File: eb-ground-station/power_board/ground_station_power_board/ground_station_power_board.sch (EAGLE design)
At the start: 73 parts, among them J1 CONN_20X2SHROUDED, Q1 SQJ459EP_MOSFET_P_CHAN, Q15 DMN61D8LVT-DUAL-N-CHANNEL-MOS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, Q17 DMN61D8LVT-DUAL-N-CHANNEL-MOS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, Q18 DMN61D8LVT-DUAL-N-CHANNEL-MOS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, Q2 SQJ459EP_MOSFET_P_CHAN, Q22 TC4427-FET-GATE-DRVR, Q23 TC4427-FET-GATE-DRVR, Q24 TC4427-FET-GATE-DRVR, Q3 SQJ459EP_MOSFET_P_CHAN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

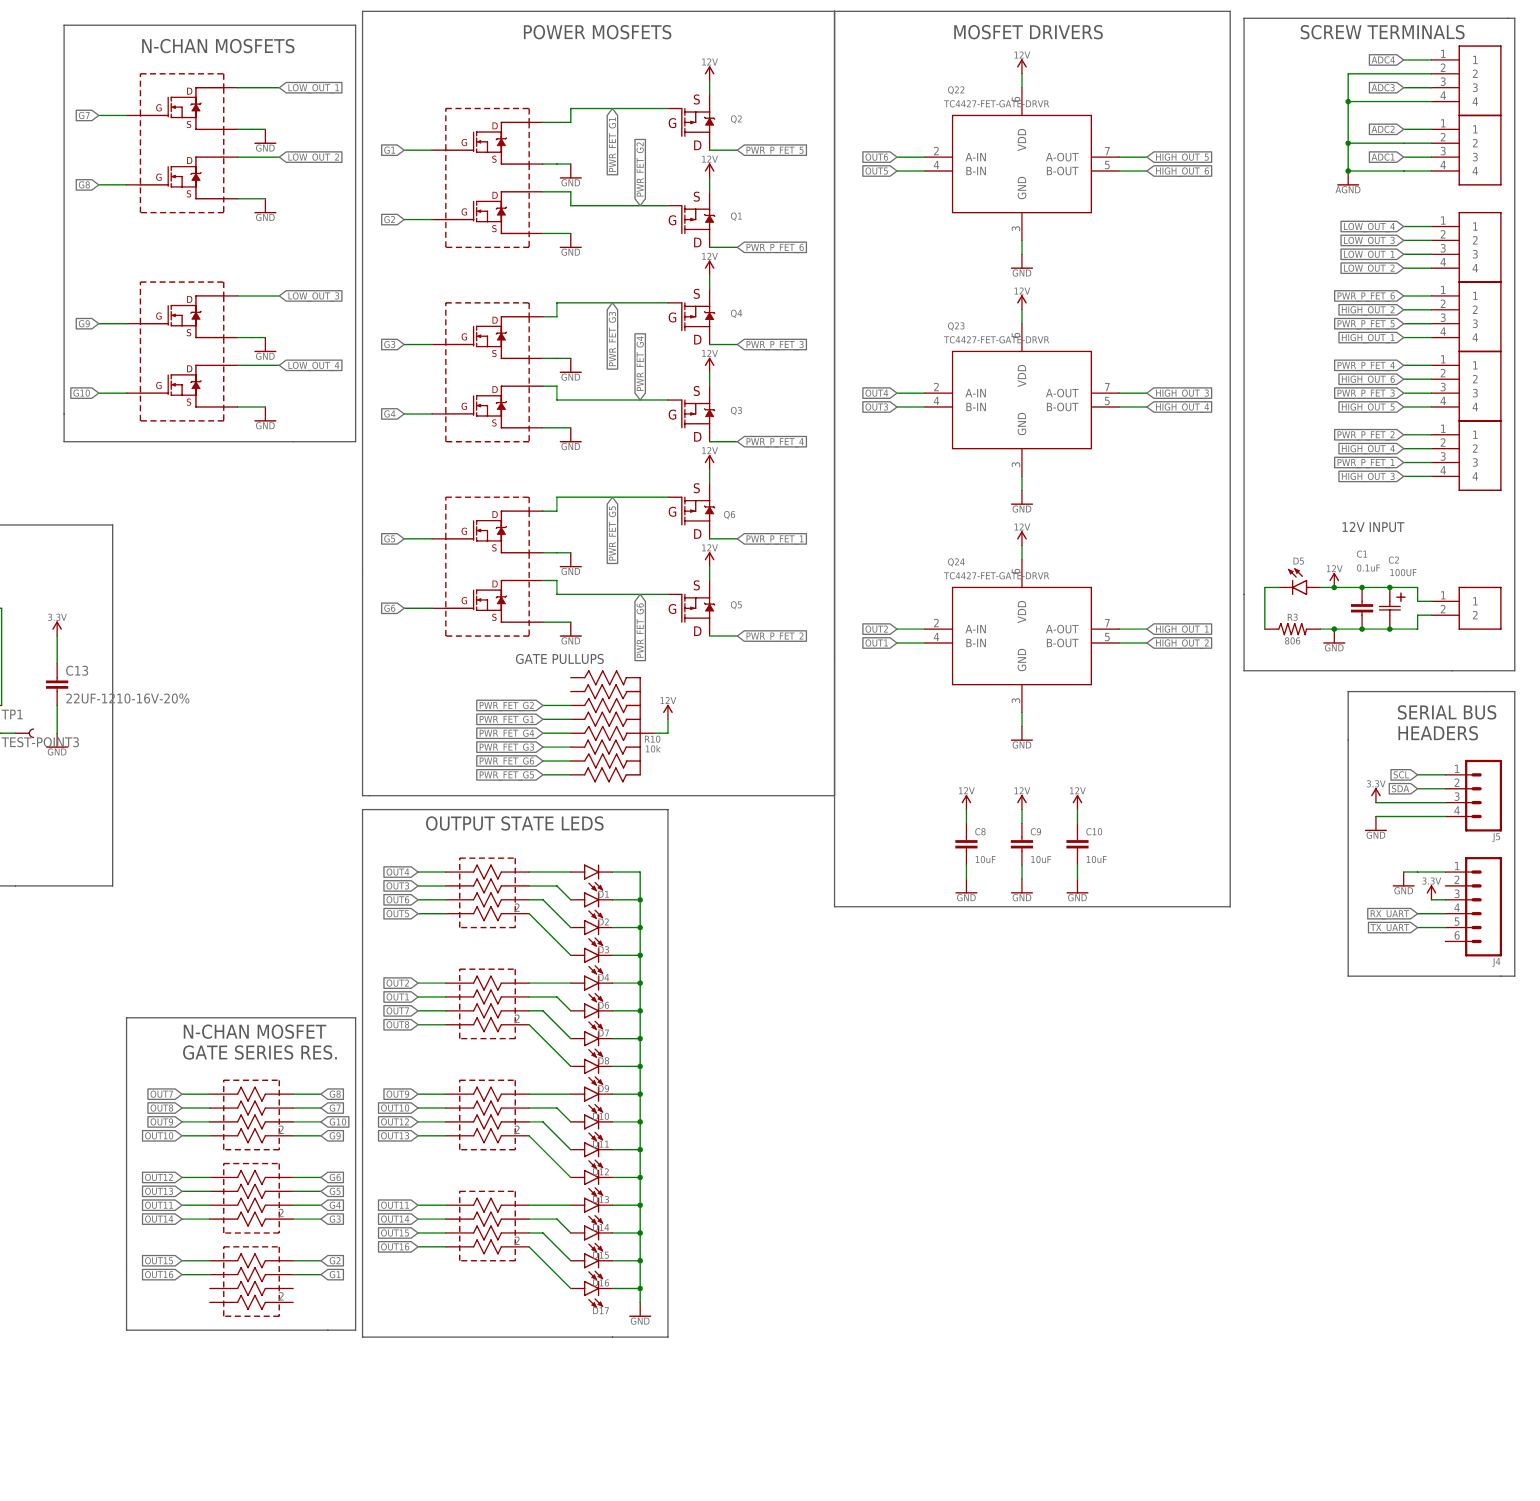
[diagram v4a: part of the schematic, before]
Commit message: Updated for 2  5V mosfets
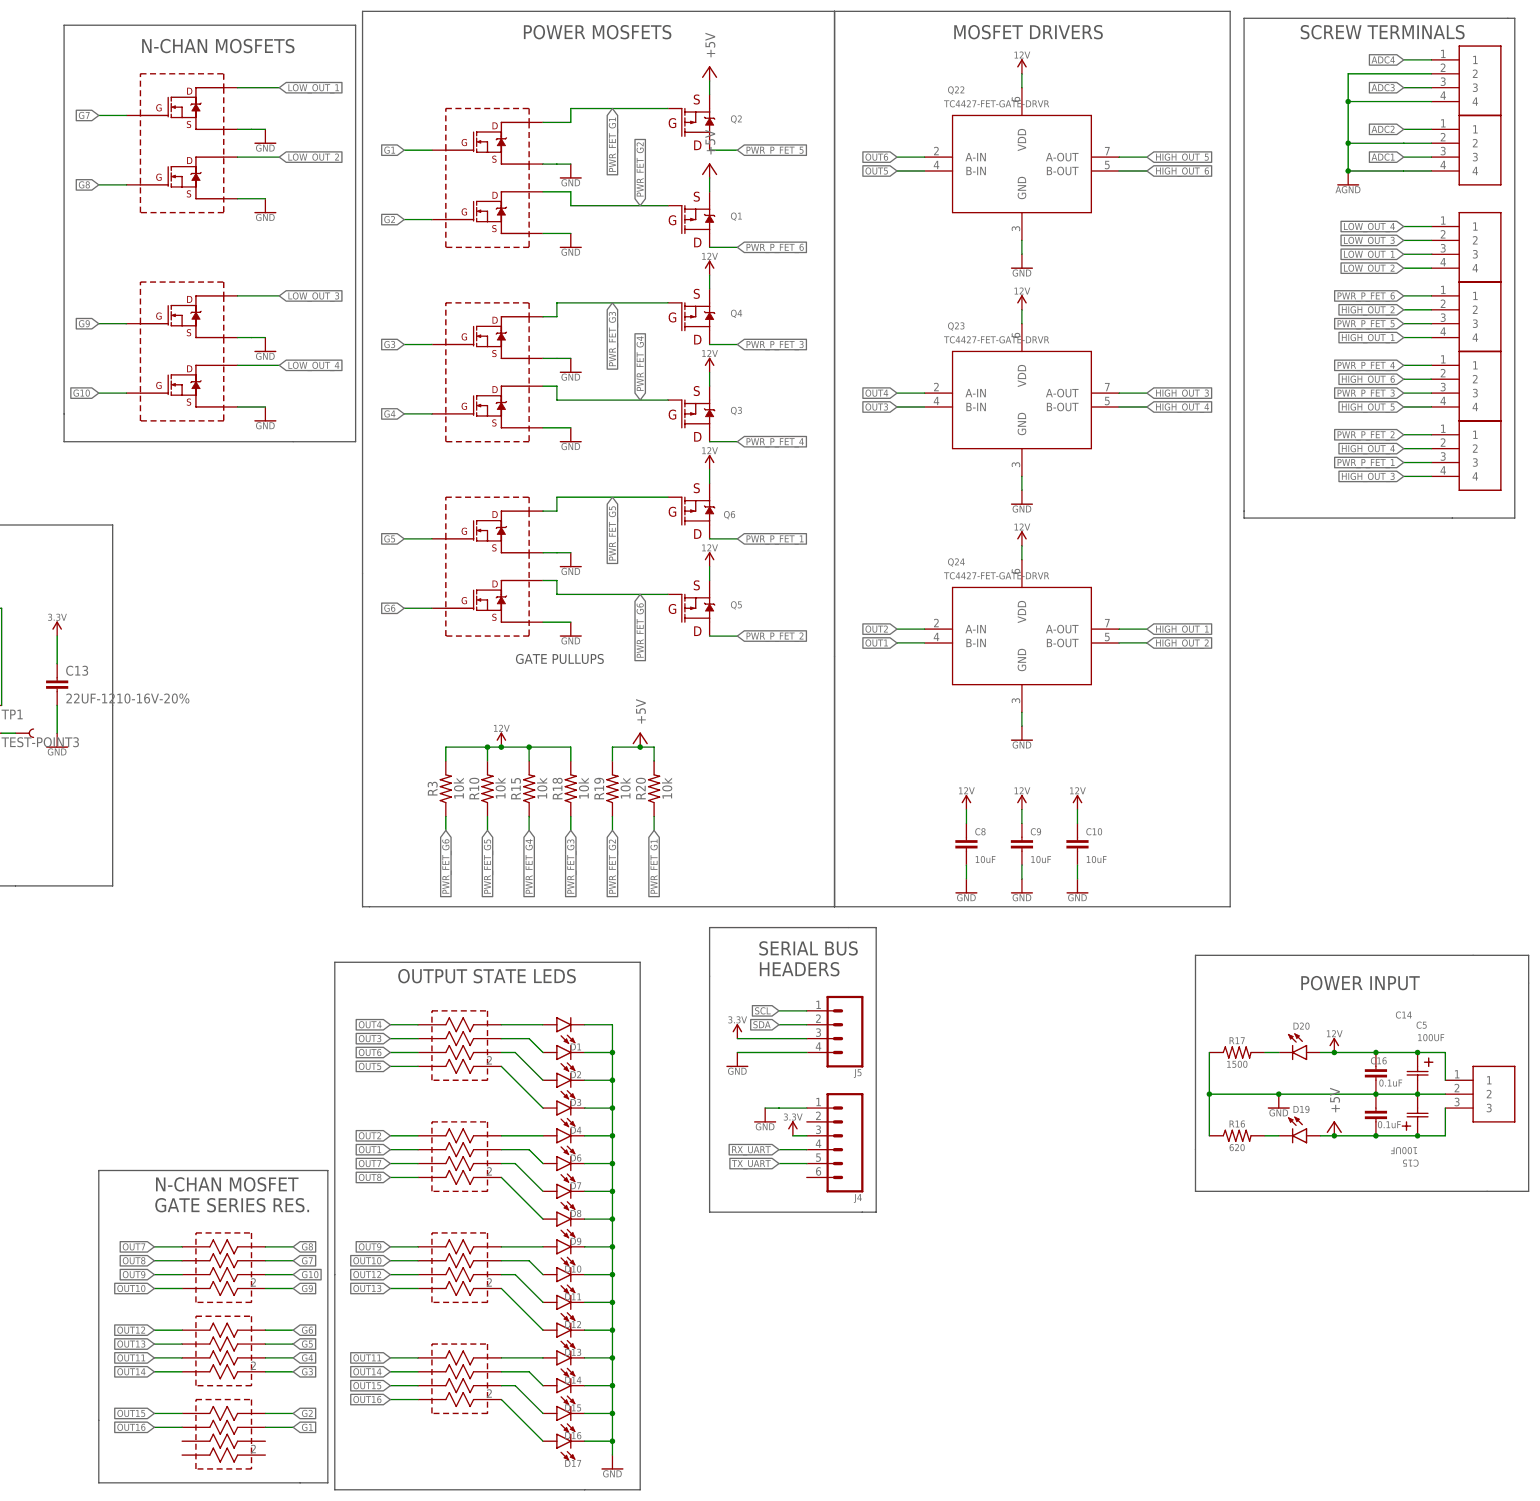
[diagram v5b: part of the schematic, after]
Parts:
- removed C1: 0.1uF, SparkFun-Capacitors:0.1UF-0603-25V-5%
- removed C2: 100UF, GROUND-STATION-POWER-BOARD:100UF-CAP-EMVH630ARA101MKE0SCHEMI-KE0-M
- removed D5: (no value), SparkFun-LED:LED0603
- removed U$7: 1714955-PHONEIX-CONTACT-TERMINAL-BLOCK, GROUND-STATION-POWER-BOARD:1714955-PHONEIX-CONTACT-TERMINAL-BLOCK
- added C14, C16: 0.1uF, SparkFun-Capacitors:0.1UF-0603-25V-5%
- added C15, C5: 100UF, GROUND-STATION-POWER-BOARD:100UF-CAP-EMVH630ARA101MKE0SCHEMI-KE0-M
- added D19, D20: (no value), SparkFun-LED:LED0603
- added R15, R18, R19, R20: 10k, SparkFun-Resistors:10KOHM-0603-1/10W-1%
- added R16: 620, SparkFun-Resistors:4.7KOHM-0603-1/10W-1%
- added R17: 1500, SparkFun-Resistors:4.7KOHM-0603-1/10W-1%
- added U$11: 1714968-PHONEIX-CONTACT-TERMINAL-BLOCK, GROUND-STATION-POWER-BOARD:1714968-PHONEIX-CONTACT-TERMINAL-BLOCK
- R10: device temp-lib:EXB-A10P391JC_ARRAY_EXBA-M -> SparkFun-Resistors:10KOHM-0603-1/10W-1%
- R3: value 806 -> 10k; device SparkFun-Resistors:4.7KOHM-0603-1/10W-1% -> SparkFun-Resistors:10KOHM-0603-1/10W-1%
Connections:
- removed net N$9: D5.C, R3.1
- new net +5V: C15.11, C16.2, D19.A, Q1.S, Q2.S, R19.2, R20.2, U$11.3
- new net N$12: D19.C, R16.2
- new net N$18: D20.C, R17.2
- net 12V: now also C14.1, C5.11, D20.A, R10.2, R15.2, R18.2, R3.2, U$11.1; no longer C1.1, C2.11, D5.A, Q1.S, Q2.S, R10.55, U$7.1
- net GND: now also C14.2, C15.22, C16.1, C5.22, R16.1, R17.1, U$11.2; no longer C1.2, C2.22, R3.2, U$7.2
- net PWR_FET_G1: now also R20.1; no longer R10.88
- net PWR_FET_G2: now also R19.1; no longer R10.22
- net PWR_FET_G3: now also R18.1; no longer R10.77
- net PWR_FET_G4: now also R15.1; no longer R10.33
- net PWR_FET_G5: now also R10.1; no longer R10.66
- net PWR_FET_G6: now also R3.1; no longer R10.44
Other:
- note added: "POWER INPUT"
- note removed: "12V INPUT"
- moved on the sheet: D1, D10, D11, D12, D13, D14, D15, D16, D17, D2, D3, D4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
